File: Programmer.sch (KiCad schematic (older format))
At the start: 10 parts, among them J1 USB_B_Micro, J2 Conn_02x05_Odd_Even, SW1 SW_Push, U1 MKL04Z32VLC4, U2 ADP2108AUJ-3.3

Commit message: Rounded corners, added LED
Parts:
- added D1: LED, LED_SMD:LED_0805_2012Metric_Pad1.15x1.40mm_HandSolder, symbol Device:LED
- added R3: 500, Resistor_SMD:R_0805_2012Metric_Pad1.15x1.40mm_HandSolder, symbol Device:R_US
- R1, R2: value R_US -> 33
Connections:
- net +3V3: now also D1.2 (A)
- net GND: now also R3.2
- new net: D1.1 (K), R3.1
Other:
- moved on the sheet: C1, C2, J1, J2, L1, R1, R2, SW1, U1, U2

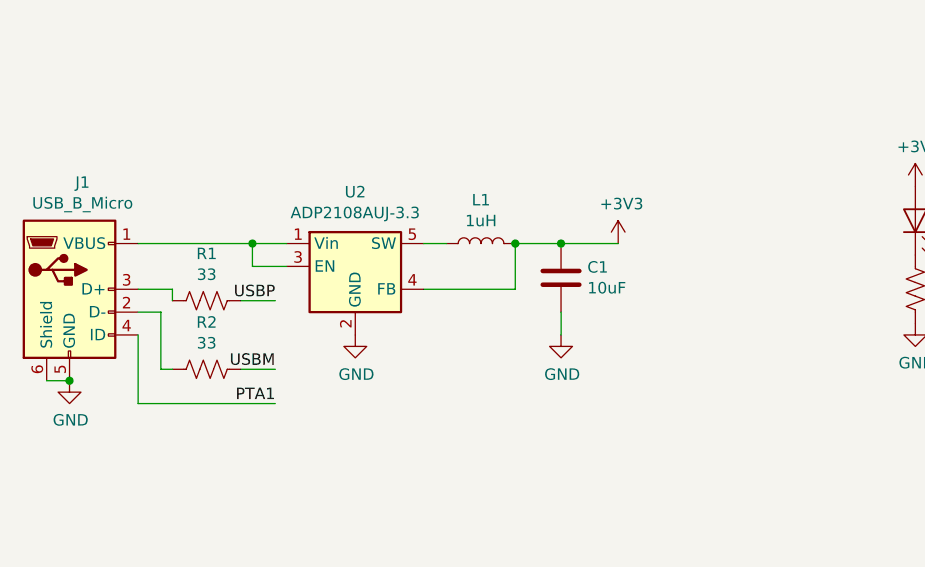
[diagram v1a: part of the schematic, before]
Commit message: Add input cap
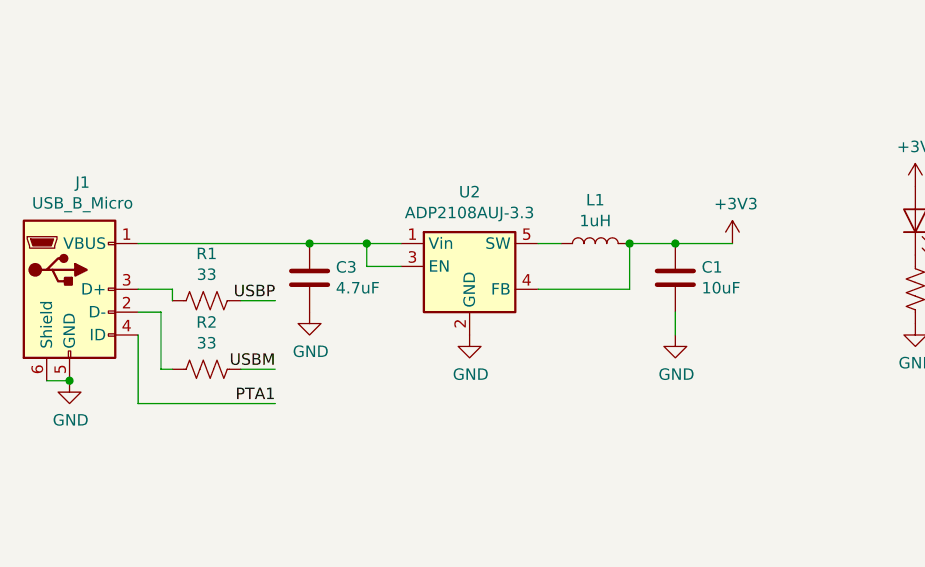
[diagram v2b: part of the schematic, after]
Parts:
- added C3: 4.7uF, Capacitor_SMD:C_0805_2012Metric_Pad1.15x1.40mm_HandSolder, symbol Device:C
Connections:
- net GND: now also C3.2
- net at J1.1 (VBUS), U2.1 (Vin), U2.3 (EN): now also C3.1
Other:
- moved on the sheet: C1, L1, U2
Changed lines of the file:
@@
 L Regulator_Switching:ADP2108AUJ-3.3 U2
 U 1 1 60041CE7
-P 2900 2550
-F 0 "U2" H 2900 2875 50  0000 C CNN
-F 1 "ADP2108AUJ-3.3" H 2900 2784 50  0000 C CNN
-F 2 "Package_TO_SOT_SMD:TSOT-23-5" H 2950 2300 50  0001 L CNN
-F 3 "https://www.analog.com/media/en/technical-documentation/data-sheets/ADP2108.pdf" H 2650 2200 50  0001 C CNN
-	1    2900 2550
+P 3400 2550
+F 0 "U2" H 3400 2875 50  0000 C CNN
+F 1 "ADP2108AUJ-3.3" H 3400 2784 50  0000 C CNN
+F 2 "Package_TO_SOT_SMD:TSOT-23-5" H 3450 2300 50  0001 L CNN
+F 3 "https://www.analog.com/media/en/technical-documentation/data-sheets/ADP2108.pdf" H 3150 2200 50  0001 C CNN
+	1    3400 2550
 	1    0    0    -1
 $EndComp
@@
 L power:GND #PWR0101
 U 1 1 60043CD3
-P 2900 2850
-F 0 "#PWR0101" H 2900 2600 50  0001 C CNN
-F 1 "GND" H 2905 2677 50  0000 C CNN
-F 2 "" H 2900 2850 50  0001 C CNN
-F 3 "" H 2900 2850 50  0001 C CNN
-	1    2900 2850
+P 3400 2850
+F 0 "#PWR0101" H 3400 2600 50  0001 C CNN
+F 1 "GND" H 3405 2677 50  0000 C CNN
+F 2 "" H 3400 2850 50  0001 C CNN
+F 3 "" H 3400 2850 50  0001 C CNN
+	1    3400 2850
 	1    0    0    -1
 $EndComp
@@
 	1550 3050 1650 3050
 Connection ~ 1650 3050
-Wire Wire Line
-	1950 2450 2450 2450
 $Comp
 L Device:L L1
 U 1 1 6004A97D
-P 3450 2450
-F 0 "L1" V 3640 2450 50  0000 C CNN
-F 1 "1uH" V 3549 2450 50  0000 C CNN
-F 2 "Inductor_SMD:L_0805_2012Metric_Pad1.15x1.40mm_HandSolder" H 3450 2450 50  0001 C CNN
-F 3 "~" H 3450 2450 50  0001 C CNN
-	1    3450 2450
+P 3950 2450
+F 0 "L1" V 4140 2450 50  0000 C CNN
+F 1 "1uH" V 4049 2450 50  0000 C CNN
+F 2 "Inductor_SMD:L_0805_2012Metric_Pad1.15x1.40mm_HandSolder" H 3950 2450 50  0001 C CNN
+F 3 "~" H 3950 2450 50  0001 C CNN
+	1    3950 2450
 	0    -1   -1   0
 $EndComp
 Wire Wire Line
-	3200 2450 3300 2450
-Wire Wire Line
-	3600 2450 3600 2650
-Wire Wire Line
-	3600 2650 3200 2650
+	3700 2450 3800 2450
+Wire Wire Line
+	4100 2450 4100 2650
+Wire Wire Line
+	4100 2650 3700 2650
 $Comp
 L Device:C C1
 U 1 1 6004C50F
-P 3800 2600
-F 0 "C1" H 3915 2646 50  0000 L CNN
-F 1 "10uF" H 3915 2555 50  0000 L CNN
-F 2 "Capacitor_SMD:C_0805_2012Metric_Pad1.15x1.40mm_HandSolder" H 3838 2450 50  0001 C CNN
-F 3 "~" H 3800 2600 50  0001 C CNN
-	1    3800 2600
+P 4300 2600
+F 0 "C1" H 4415 2646 50  0000 L CNN
+F 1 "10uF" H 4415 2555 50  0000 L CNN
+F 2 "Capacitor_SMD:C_0805_2012Metric_Pad1.15x1.40mm_HandSolder" H 4338 2450 50  0001 C CNN
+F 3 "~" H 4300 2600 50  0001 C CNN
+	1    4300 2600
 	1    0    0    -1
 $EndComp
@@
 L power:GND #PWR0103
 U 1 1 6004CE89
-P 3800 2850
-F 0 "#PWR0103" H 3800 2600 50  0001 C CNN
-F 1 "GND" H 3805 2677 50  0000 C CNN
-F 2 "" H 3800 2850 50  0001 C CNN
-F 3 "" H 3800 2850 50  0001 C CNN
-	1    3800 2850
-	1    0    0    -1
-$EndComp
-Wire Wire Line
-	3600 2450 3800 2450
-Connection ~ 3600 2450
-Connection ~ 3800 2450
-Wire Wire Line
-	3800 2450 4050 2450
-Wire Wire Line
-	3800 2750 3800 2850
+P 4300 2850
+F 0 "#PWR0103" H 4300 2600 50  0001 C CNN
+F 1 "GND" H 4305 2677 50  0000 C CNN
+F 2 "" H 4300 2850 50  0001 C CNN
+F 3 "" H 4300 2850 50  0001 C CNN
+	1    4300 2850
+	1    0    0    -1
+$EndComp
+Wire Wire Line
+	4100 2450 4300 2450
+Connection ~ 4100 2450
+Connection ~ 4300 2450
+Wire Wire Line
+	4300 2450 4550 2450
+Wire Wire Line
+	4300 2750 4300 2850
 $Comp
 L power:+3V3 #PWR0104
 U 1 1 6004E2FC
-P 4050 2450
-F 0 "#PWR0104" H 4050 2300 50  0001 C CNN
-F 1 "+3V3" H 4065 2623 50  0000 C CNN
-F 2 "" H 4050 2450 50  0001 C CNN
-F 3 "" H 4050 2450 50  0001 C CNN
-	1    4050 2450
-	1    0    0    -1
-$EndComp
-Wire Wire Line
-	2600 2550 2450 2550
-Wire Wire Line
-	2450 2550 2450 2450
-Connection ~ 2450 2450
-Wire Wire Line
-	2450 2450 2600 2450
+P 4550 2450
+F 0 "#PWR0104" H 4550 2300 50  0001 C CNN
+F 1 "+3V3" H 4565 2623 50  0000 C CNN
+F 2 "" H 4550 2450 50  0001 C CNN
+F 3 "" H 4550 2450 50  0001 C CNN
+	1    4550 2450
+	1    0    0    -1
+$EndComp
+Wire Wire Line
+	3100 2550 2950 2550
+Wire Wire Line
+	2950 2550 2950 2450
+Wire Wire Line
+	2950 2450 3100 2450
 $Comp
 L Device:R_US R1
@@
 	1    0    0    -1
 $EndComp
+$Comp
+L Device:C C3
+U 1 1 601A6D50
+P 2700 2600
+F 0 "C3" H 2815 2646 50  0000 L CNN
+F 1 "4.7uF" H 2815 2555 50  0000 L CNN
+F 2 "Capacitor_SMD:C_0805_2012Metric_Pad1.15x1.40mm_HandSolder" H 2738 2450 50  0001 C CNN
+F 3 "~" H 2700 2600 50  0001 C CNN
+	1    2700 2600
+	1    0    0    -1
+$EndComp
+Connection ~ 2950 2450
+$Comp
+L power:GND #PWR0114
+U 1 1 601B11F4
+P 2700 2750
+F 0 "#PWR0114" H 2700 2500 50  0001 C CNN
+F 1 "GND" H 2705 2577 50  0000 C CNN
+F 2 "" H 2700 2750 50  0001 C CNN
+F 3 "" H 2700 2750 50  0001 C CNN
+	1    2700 2750
+	1    0    0    -1
+$EndComp
+Wire Wire Line
+	1950 2450 2700 2450
+Connection ~ 2700 2450
+Wire Wire Line
+	2700 2450 2950 2450
 $EndSCHEMATC

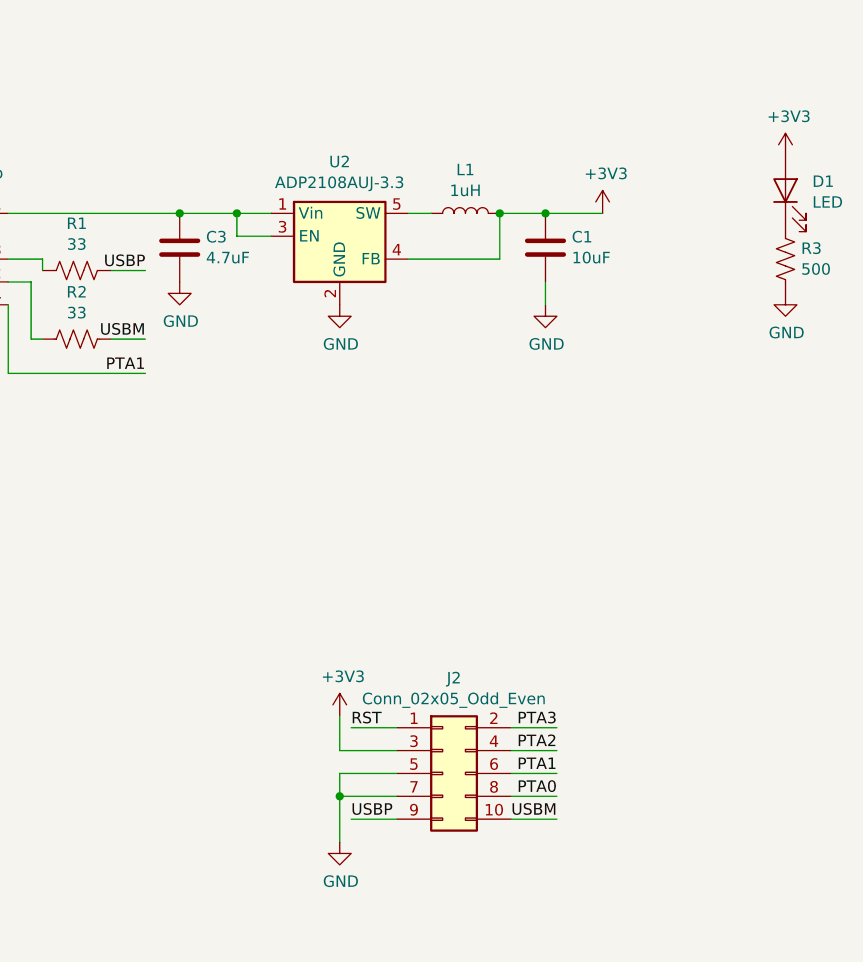
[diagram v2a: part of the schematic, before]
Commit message: Provide 5v to target
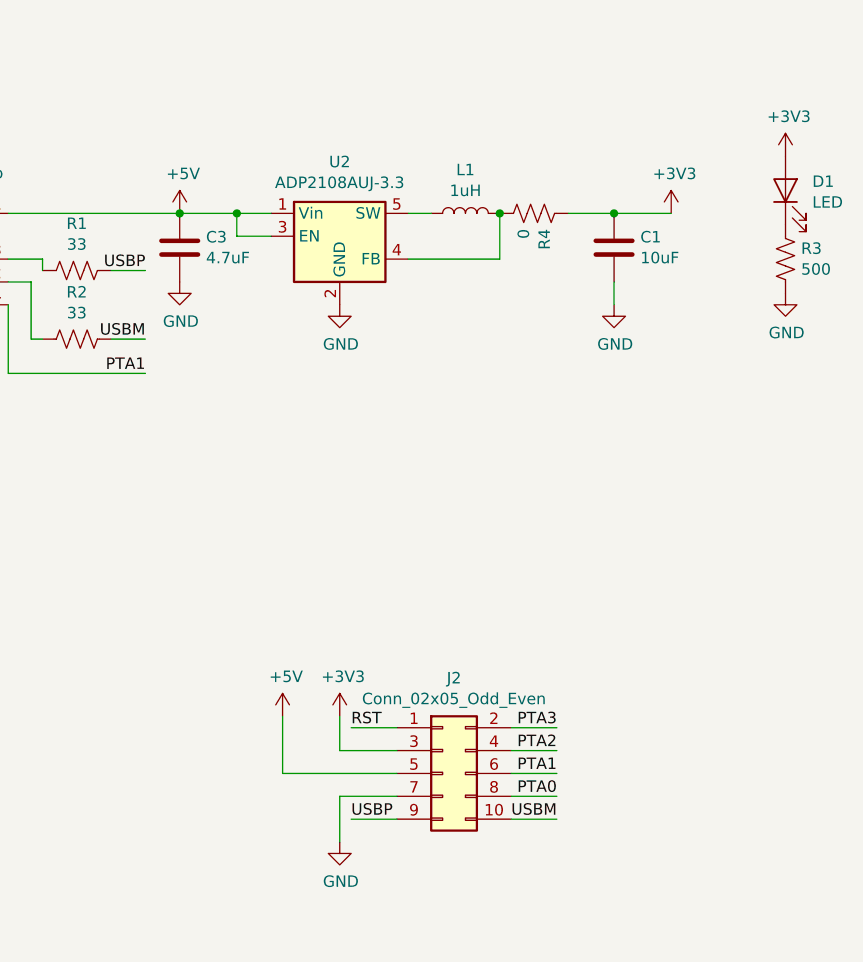
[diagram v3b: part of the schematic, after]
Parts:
- added R4: 0, Resistor_SMD:R_0805_2012Metric_Pad1.15x1.40mm_HandSolder, symbol Device:R_US
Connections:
- net +3V3: now also R4.1; no longer L1.2, U2.4 (FB)
- net GND: no longer J2.5 (Pin_5)
- net +5V: now reaches C3.1, J1.1 (VBUS), U2.1 (Vin), U2.3 (EN)
- net +5V: now also J2.5 (Pin_5)
- new net: L1.2, R4.2, U2.4 (FB)
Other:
- moved on the sheet: C1
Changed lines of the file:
@@
 L Device:C C1
 U 1 1 6004C50F
-P 4300 2600
-F 0 "C1" H 4415 2646 50  0000 L CNN
-F 1 "10uF" H 4415 2555 50  0000 L CNN
-F 2 "Capacitor_SMD:C_0805_2012Metric_Pad1.15x1.40mm_HandSolder" H 4338 2450 50  0001 C CNN
-F 3 "~" H 4300 2600 50  0001 C CNN
-	1    4300 2600
+P 4600 2600
+F 0 "C1" H 4715 2646 50  0000 L CNN
+F 1 "10uF" H 4715 2555 50  0000 L CNN
+F 2 "Capacitor_SMD:C_0805_2012Metric_Pad1.15x1.40mm_HandSolder" H 4638 2450 50  0001 C CNN
+F 3 "~" H 4600 2600 50  0001 C CNN
+	1    4600 2600
 	1    0    0    -1
 $EndComp
@@
 L power:GND #PWR0103
 U 1 1 6004CE89
-P 4300 2850
-F 0 "#PWR0103" H 4300 2600 50  0001 C CNN
-F 1 "GND" H 4305 2677 50  0000 C CNN
-F 2 "" H 4300 2850 50  0001 C CNN
-F 3 "" H 4300 2850 50  0001 C CNN
-	1    4300 2850
-	1    0    0    -1
-$EndComp
-Wire Wire Line
-	4100 2450 4300 2450
-Connection ~ 4100 2450
-Connection ~ 4300 2450
-Wire Wire Line
-	4300 2450 4550 2450
-Wire Wire Line
-	4300 2750 4300 2850
+P 4600 2850
+F 0 "#PWR0103" H 4600 2600 50  0001 C CNN
+F 1 "GND" H 4605 2677 50  0000 C CNN
+F 2 "" H 4600 2850 50  0001 C CNN
+F 3 "" H 4600 2850 50  0001 C CNN
+	1    4600 2850
+	1    0    0    -1
+$EndComp
+Wire Wire Line
+	4400 2450 4600 2450
+Connection ~ 4600 2450
+Wire Wire Line
+	4600 2450 4850 2450
+Wire Wire Line
+	4600 2750 4600 2850
 $Comp
 L power:+3V3 #PWR0104
 U 1 1 6004E2FC
-P 4550 2450
-F 0 "#PWR0104" H 4550 2300 50  0001 C CNN
-F 1 "+3V3" H 4565 2623 50  0000 C CNN
-F 2 "" H 4550 2450 50  0001 C CNN
-F 3 "" H 4550 2450 50  0001 C CNN
-	1    4550 2450
+P 4850 2450
+F 0 "#PWR0104" H 4850 2300 50  0001 C CNN
+F 1 "+3V3" H 4865 2623 50  0000 C CNN
+F 2 "" H 4850 2450 50  0001 C CNN
+F 3 "" H 4850 2450 50  0001 C CNN
+	1    4850 2450
 	1    0    0    -1
 $EndComp
@@
 Wire Wire Line
 	3400 5000 3650 5000
-Wire Wire Line
-	3400 4900 3650 4900
-Wire Wire Line
-	3400 4900 3400 5000
 $Comp
 L power:GND #PWR0109
@@
 	1    0    0    -1
 $EndComp
-Connection ~ 3400 5000
 $Comp
 L power:+3V3 #PWR0110
@@
 Wire Wire Line
 	2700 2450 2950 2450
+$Comp
+L power:+5V #PWR0115
+U 1 1 601CA9CB
+P 2700 2450
+F 0 "#PWR0115" H 2700 2300 50  0001 C CNN
+F 1 "+5V" H 2715 2623 50  0000 C CNN
+F 2 "" H 2700 2450 50  0001 C CNN
+F 3 "" H 2700 2450 50  0001 C CNN
+	1    2700 2450
+	1    0    0    -1
+$EndComp
+$Comp
+L power:+5V #PWR0116
+U 1 1 601CB73C
+P 3150 4650
+F 0 "#PWR0116" H 3150 4500 50  0001 C CNN
+F 1 "+5V" H 3165 4823 50  0000 C CNN
+F 2 "" H 3150 4650 50  0001 C CNN
+F 3 "" H 3150 4650 50  0001 C CNN
+	1    3150 4650
+	1    0    0    -1
+$EndComp
+Wire Wire Line
+	3150 4650 3150 4900
+Wire Wire Line
+	3150 4900 3650 4900
+$Comp
+L Device:R_US R4
+U 1 1 6025F4F6
+P 4250 2450
+F 0 "R4" H 4318 2496 50  0000 L CNN
+F 1 "0" H 4318 2405 50  0000 L CNN
+F 2 "Resistor_SMD:R_0805_2012Metric_Pad1.15x1.40mm_HandSolder" V 4290 2440 50  0001 C CNN
+F 3 "~" H 4250 2450 50  0001 C CNN
+	1    4250 2450
+	0    1    1    0
+$EndComp
+Connection ~ 4100 2450
 $EndSCHEMATC

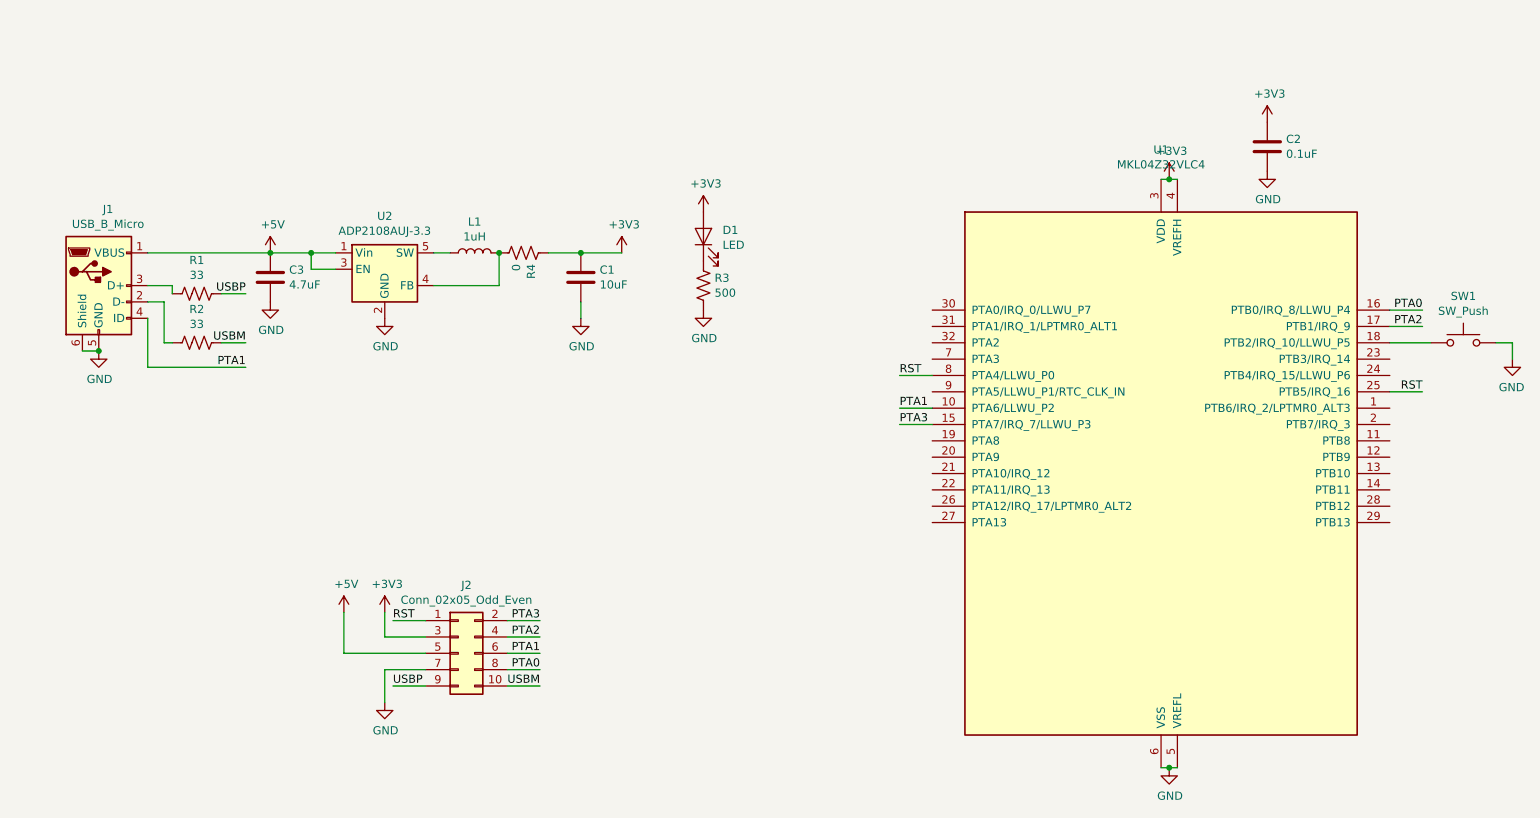
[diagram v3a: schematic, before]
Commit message: Add 0 ohm resistor to ID pin, cleanup
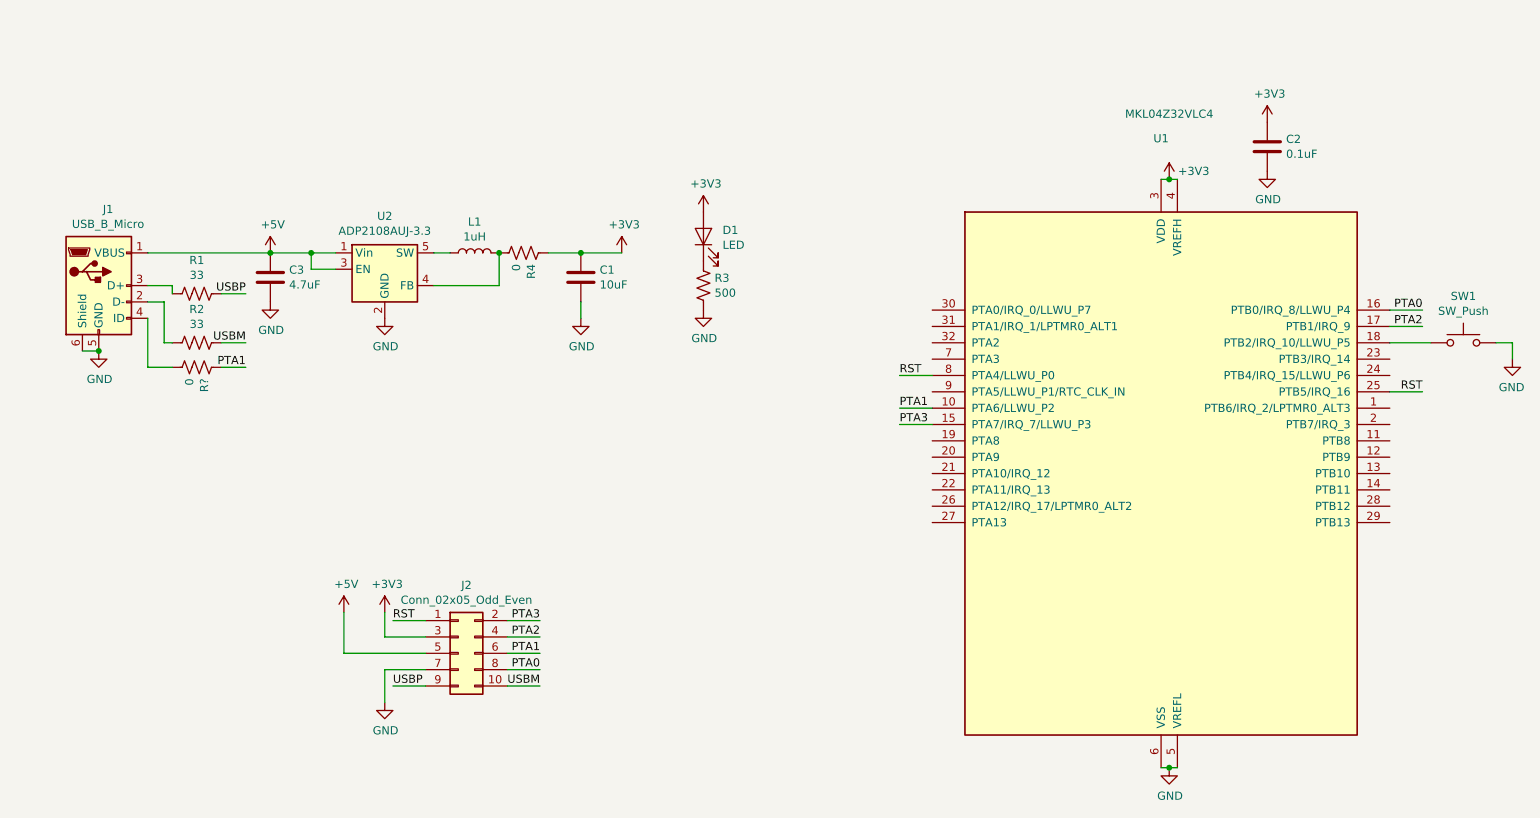
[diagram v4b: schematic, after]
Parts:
- added R?: 0, Resistor_SMD:R_0805_2012Metric_Pad1.15x1.40mm_HandSolder, symbol Device:R_US
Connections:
- net PTA1: now also R?.1; no longer J1.4 (ID)
- new net: J1.4 (ID), R?.2
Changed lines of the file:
@@
 U 1 1 6003A1DD
 P 8150 3800
-F 0 "U1" H 8150 5781 50  0000 C CNN
-F 1 "MKL04Z32VLC4" H 8150 5690 50  0000 C CNN
+F 0 "U1" H 8150 5850 50  0000 C CNN
+F 1 "MKL04Z32VLC4" H 8200 6000 50  0000 C CNN
 F 2 "Package_QFP:LQFP-32_7x7mm_P0.8mm" H 8300 2175 50  0001 L TNN
 F 3 "http://www.nxp.com/docs/en/data-sheet/KL04P48M48SF1.pdf" H 8450 2000 50  0001 L BNN
@@
 P 8200 2000
 F 0 "#PWR0105" H 8200 1850 50  0001 C CNN
-F 1 "+3V3" H 8215 2173 50  0000 C CNN
+F 1 "+3V3" H 8350 2050 50  0000 C CNN
 F 2 "" H 8200 2000 50  0001 C CNN
 F 3 "" H 8200 2000 50  0001 C CNN
@@
 Text Label 2550 3000 2    50   ~ 0
 USBM
-Wire Wire Line
-	1950 3150 2550 3150
 Text Label 2550 3150 2    50   ~ 0
 PTA1
@@
 $EndComp
 Connection ~ 4100 2450
+$Comp
+L Device:R_US R?
+U 1 1 602B701D
+P 2250 3150
+F 0 "R?" H 2318 3196 50  0000 L CNN
+F 1 "0" H 2318 3105 50  0000 L CNN
+F 2 "Resistor_SMD:R_0805_2012Metric_Pad1.15x1.40mm_HandSolder" V 2290 3140 50  0001 C CNN
+F 3 "~" H 2250 3150 50  0001 C CNN
+	1    2250 3150
+	0    1    1    0
+$EndComp
+Wire Wire Line
+	1950 3150 2100 3150
+Wire Wire Line
+	2400 3150 2550 3150
 $EndSCHEMATC

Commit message: Annotate
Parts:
- gave numbers to parts that had none: 1
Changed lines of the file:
@@
 Connection ~ 4100 2450
 $Comp
-L Device:R_US R?
+L Device:R_US R5
 U 1 1 602B701D
 P 2250 3150
-F 0 "R?" H 2318 3196 50  0000 L CNN
+F 0 "R5" H 2318 3196 50  0000 L CNN
 F 1 "0" H 2318 3105 50  0000 L CNN
 F 2 "Resistor_SMD:R_0805_2012Metric_Pad1.15x1.40mm_HandSolder" V 2290 3140 50  0001 C CNN
